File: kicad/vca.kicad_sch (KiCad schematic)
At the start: 29 parts, among them Q1 BC549C, Q2 BC549C, Q3 BC549C, Q4 BC549C, Q5 BC549C, Q6 BC549C, Q7 BC549C, Q8 BC549C, Q9 BC549C, U1 NE5532

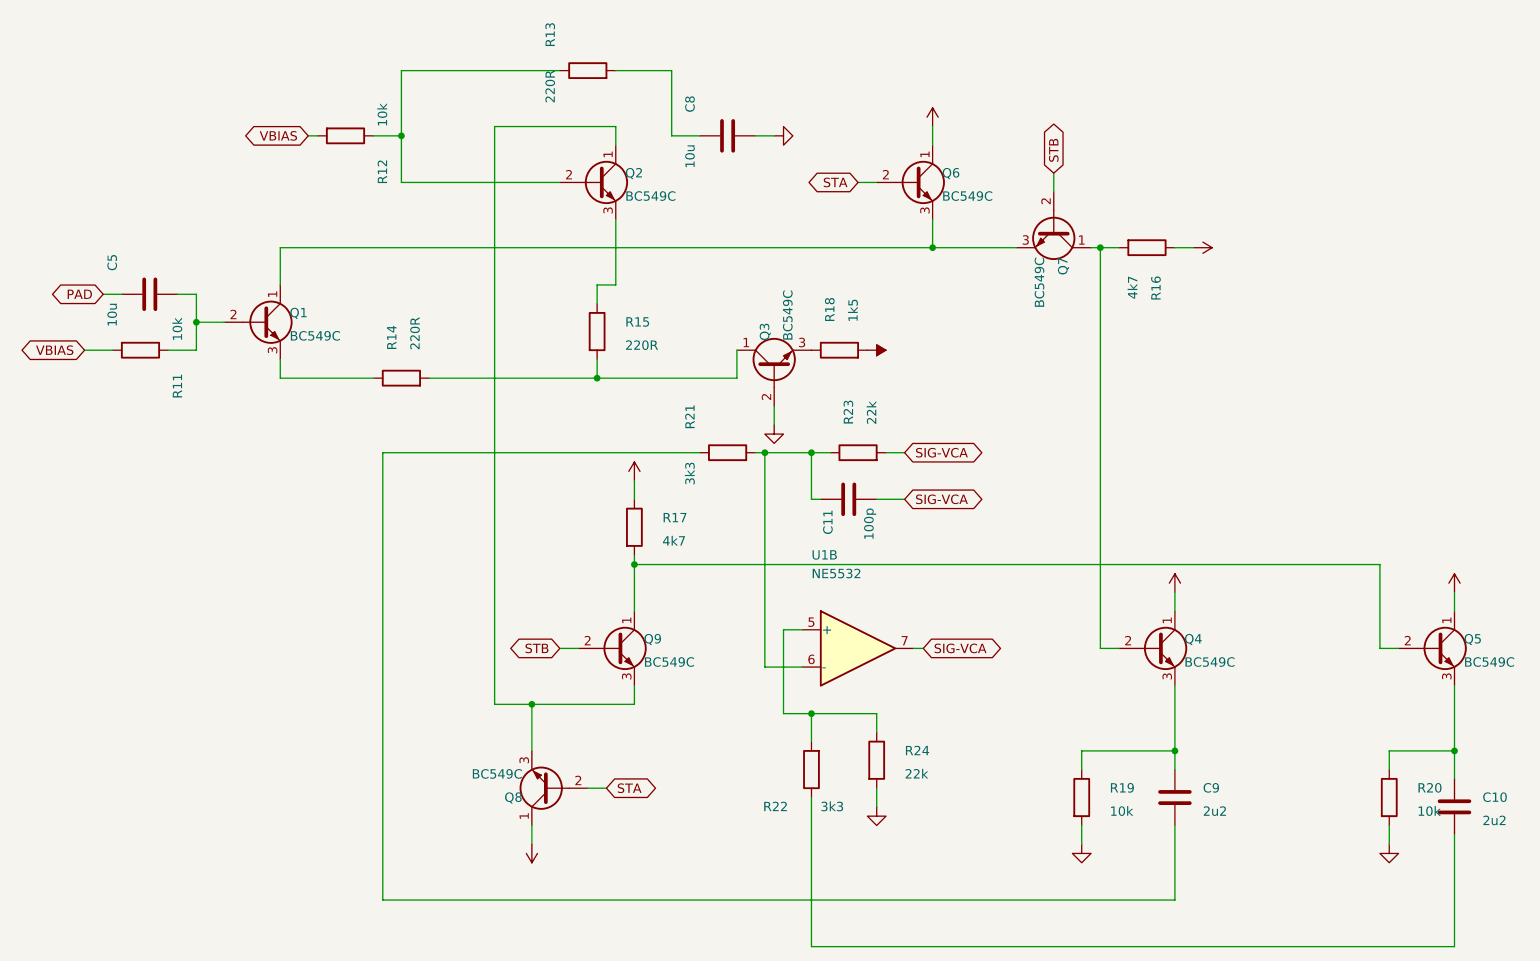
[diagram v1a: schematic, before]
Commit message: Add reorganised schematic to split files.
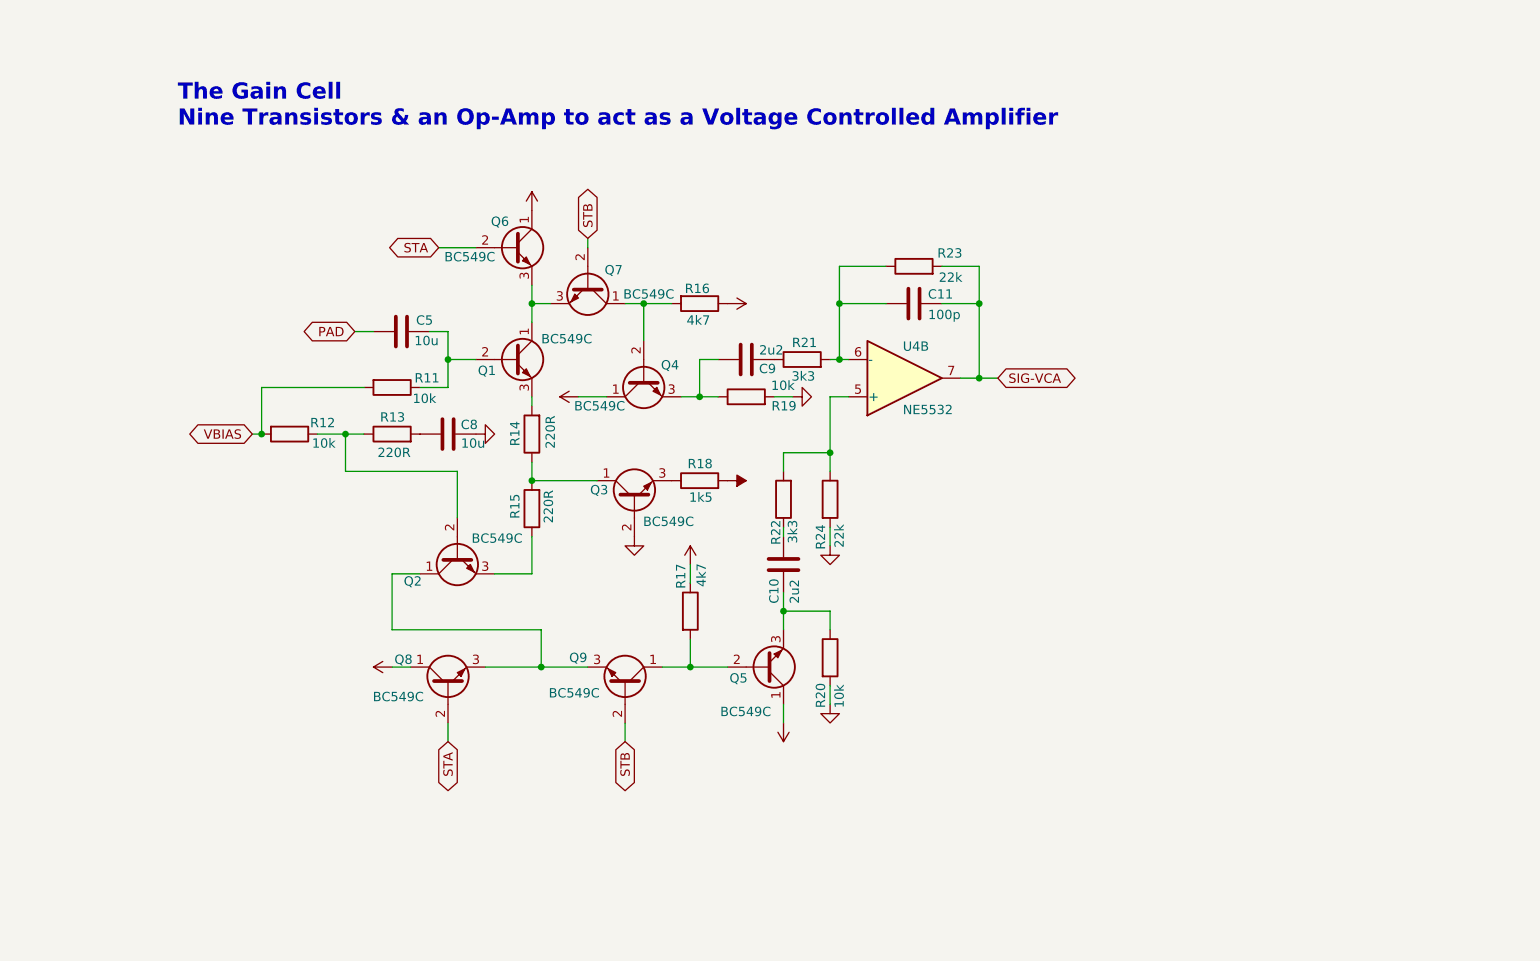
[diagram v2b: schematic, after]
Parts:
- removed U1: NE5532, Package_DIP:DIP-8_W7.62mm, symbol Amplifier_Operational:NE5532
- added U4: NE5532, Package_DIP:DIP-8_W7.62mm_Socket, symbol Amplifier_Operational:NE5532
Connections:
- net SIG-VCA: now also U4.7
- net at C11.1, R21.2, R23.1: now also U4.6 (-)
- net at Q3.1 (C), R15.2: now also R14.1; no longer R14.2
- net at Q5.3 (E), R20.1: now also C10.2; no longer C10.1
- net at R22.1: now also C10.1; no longer C10.2
- net at R22.2, R24.1: now also U4.5 (+)
- net at Q1.3 (E): now also R14.2; no longer R14.1
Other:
- note added: "The Gain Cell Nine Transistors & an Op-Amp to act as a Voltage Controlled Amplifier"

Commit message: Match the split sheets' chip references to the board (#4)
Pasting the board schematic into the split sheets renumbered five units:
the VCA recovery amp was U4B (board U1B), the sidechain TL072 was U10
(board U4), U4's power unit was U10, U7's power unit was U11, and the
LM3915 was U12 (board U10). They now carry the board's references, so
the split sheets and compressor_with_pcb have the same 167 parts and the
same 119 nets.
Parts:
- renumbered U4 to U1
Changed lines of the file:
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@@
 		(in_pos_files yes)
 		(dnp no)
-		(property "Reference" "U4"
+		(property "Reference" "U1"
 			(at 140.716 68.072 0)
 			(show_name no)
@@
 			(project "UTS Mini Mixing Desk - Compressor"
 				(path "/fdeae63a-37f5-58fb-b342-cb68d8a6bfbc/174e7320-d7b1-5aab-af4c-021d06d87bce"
-					(reference "U4")
+					(reference "U1")
 					(unit 2)
 				)

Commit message: Bring the compressor's values in line with the design targets
Through gain: R21/R22 3k3 to 6k8 halves the recovery amp's gain, so the
module is unity balanced in to out and BYPASS matches; R36 100k to 200k
keeps the detector's level. Bass: C9/C10 2u2 to 4u7 with the larger
input resistors puts the -3 dB point near 5 Hz.
Threshold: RV3 1M linear to 250k audio taper and R35 20k to 2k4 spread
about -20 to +20 dBu over the knob. R60 47k to 24k sets the resting
steer near 150 mV.
Timing: R45/R46/RV5 and R47/RV6/R74 scaled up to match the RC targets
with the same C15.

Same changes on the sheets, both boards and design.py. The simulation's
pot model gains an audio taper, and the burst test now runs at half
threshold.
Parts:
- C10, C9: value 2u2 -> 4u7
- R21, R22: value 3k3 -> 6k8
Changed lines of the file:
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@@
 			)
 		)
-		(property "Value" "3k3"
+		(property "Value" "6k8"
 			(at 125.73 91.694 90)
 			(show_name no)
@@
 			)
 		)
-		(property "Value" "2u2"
+		(property "Value" "4u7"
 			(at 124.46 68.58 90)
 			(show_name no)
@@
 			)
 		)
-		(property "Value" "3k3"
+		(property "Value" "6k8"
 			(at 128.778 72.136 90)
 			(show_name no)
@@
 			)
 		)
-		(property "Value" "2u2"
+		(property "Value" "4u7"
 			(at 125.984 103.124 90)
 			(show_name no)

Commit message: Fit real film capacitors on the main board and use Altronics pots for RV5/RV6
RV5 (ATTACK) goes 4k7 -> 10k and RV6 (RELEASE) 500k -> 1M, the nearest
Altronics 9 mm values (R1946, R1950), on the split sheets, both boards
and design.py; the Sim.Params follow (R=10000, R=1e+06).

C5, C8, C9, C10, C14, C15 and C35 were drawn as 7 x 2.5 mm on 5 mm, which
no 2.2-10 uF film part fits. They now use stock KiCad footprints for
in-stock element14 parts:
  10 uF  C5 C8 C15  TDK B32562H1106K000   C_Rect_L16.5mm_W11.8mm_P15.00mm_MKT
  4.7 uF C9 C10     TDK B32562H1475K000   C_Rect_L16.5mm_W7.3mm_P15.00mm_MKT
  2.2 uF C14 C35    KEMET MMK5225K63J06L4 C_Rect_L7.2mm_W7.2mm_P5.00mm_FKS2...

To make room, small parts were re-placed by script (the caps near their
old spots, displaced parts re-homed, then same-footprint parts swapped to
cut wire length; transistors, ICs, connectors and trimmers did not move)
and the main board was re-routed with Freerouting, keeping the original
card-finger stubs. DRC 0 errors, 0 unconnected, schematic parity clean;
ERC 0 errors. The BOM names the element14 parts.
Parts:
- C10, C9: footprint Capacitor_THT:C_Rect_L7.0mm_W2.5mm_P5.00mm -> Capacitor_THT:C_Rect_L16.5mm_W7.3mm_P15.00mm_MKT
- C5, C8: footprint Capacitor_THT:C_Rect_L7.0mm_W2.5mm_P5.00mm -> Capacitor_THT:C_Rect_L16.5mm_W11.8mm_P15.00mm_MKT
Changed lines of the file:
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@@
 			)
 		)
-		(property "Footprint" "Capacitor_THT:C_Rect_L7.0mm_W2.5mm_P5.00mm"
+		(property "Footprint" "Capacitor_THT:C_Rect_L16.5mm_W11.8mm_P15.00mm_MKT"
 			(at 78.74 80.01 0)
 			(hide yes)
@@
 			)
 		)
-		(property "Footprint" "Capacitor_THT:C_Rect_L7.0mm_W2.5mm_P5.00mm"
+		(property "Footprint" "Capacitor_THT:C_Rect_L16.5mm_W7.3mm_P15.00mm_MKT"
 			(at 119.38 69.85 0)
 			(hide yes)
@@
 			)
 		)
-		(property "Footprint" "Capacitor_THT:C_Rect_L7.0mm_W2.5mm_P5.00mm"
+		(property "Footprint" "Capacitor_THT:C_Rect_L16.5mm_W11.8mm_P15.00mm_MKT"
 			(at 72.39 66.04 0)
 			(hide yes)
@@
 			)
 		)
-		(property "Footprint" "Capacitor_THT:C_Rect_L7.0mm_W2.5mm_P5.00mm"
+		(property "Footprint" "Capacitor_THT:C_Rect_L16.5mm_W7.3mm_P15.00mm_MKT"
 			(at 124.46 97.79 0)
 			(hide yes)
